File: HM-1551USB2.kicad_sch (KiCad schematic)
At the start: 21 parts, among them Q1 IRLML6402, U1 USBLC6-2SC6, U2 FT232RL, U3 HM-MOD-UART

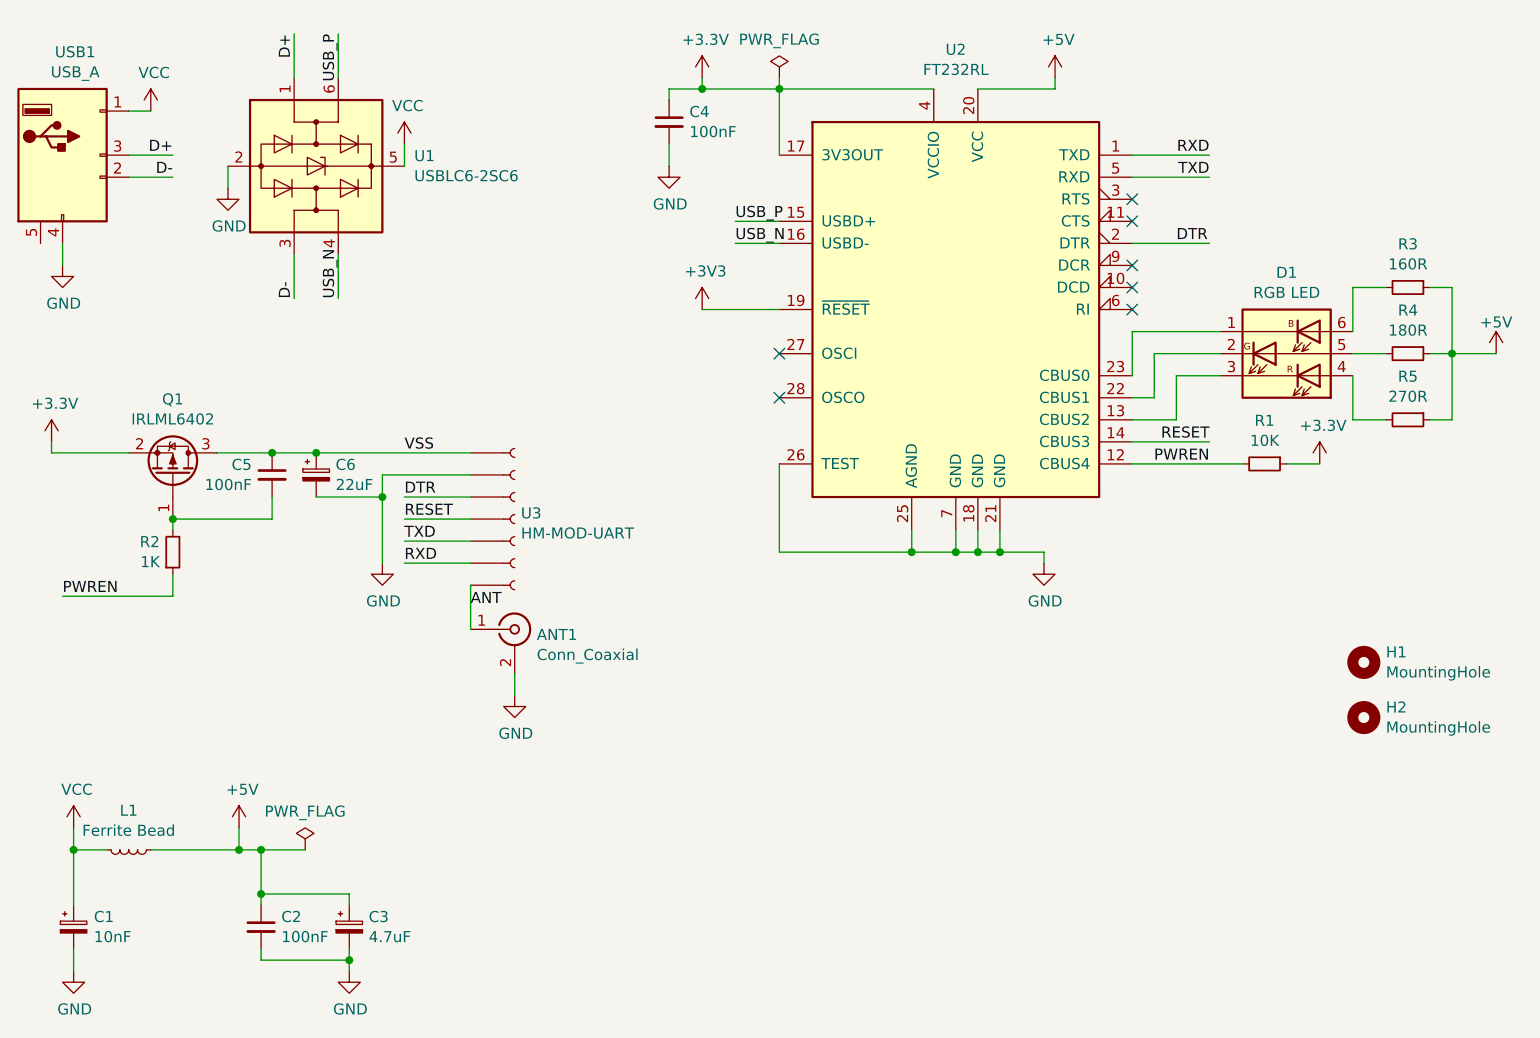
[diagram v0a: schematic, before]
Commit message: Update component properties and fill BOM
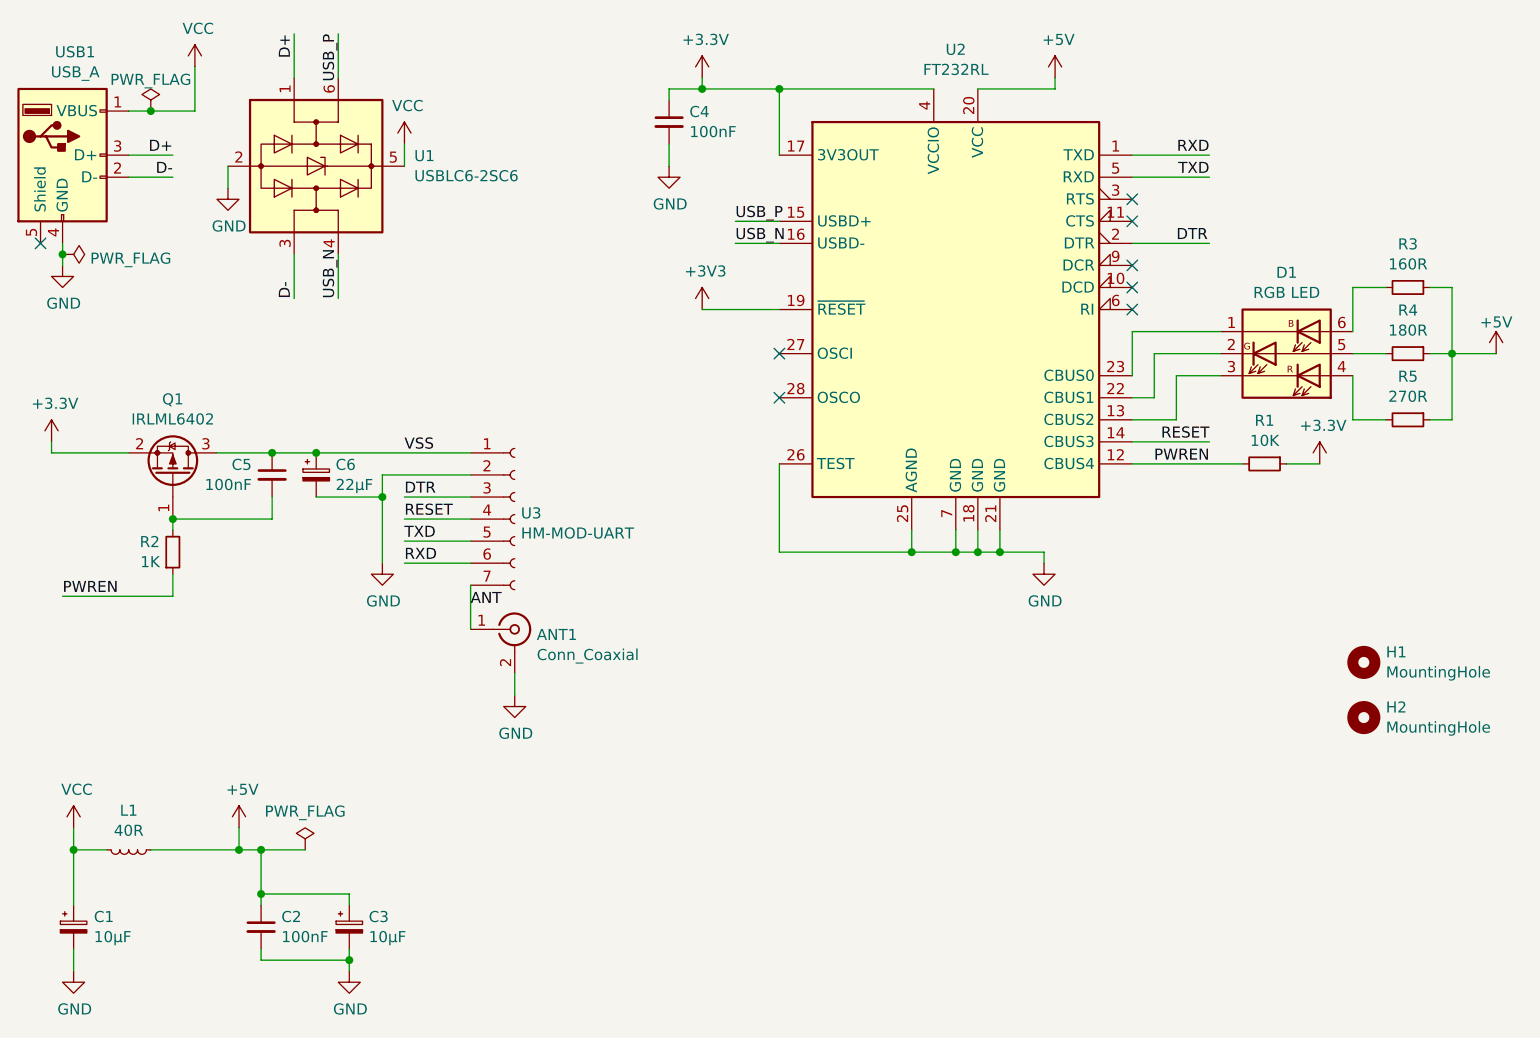
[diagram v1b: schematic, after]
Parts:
- ANT1: LCSC (none) -> C914558; PN (none) -> SMA-KE-P903
- C1: value 10nF -> 10µF; symbol Device:CP_Small -> Device:C_Polarized_Small; LCSC (none) -> C7177; PN (none) -> TAJA106K010RNJ
- C2, C4, C5: LCSC (none) -> C307360; PN (none) -> CL21B104KBFWPNE
- C3: value 4.7uF -> 10µF; symbol Device:CP_Small -> Device:C_Polarized_Small; LCSC (none) -> C7177; PN (none) -> TAJA106K010RNJ
- C6: value 22uF -> 22µF; symbol Device:CP_Small -> Device:C_Polarized_Small; LCSC (none) -> C130377; PN (none) -> 293D226X9016C2TE3
- D1: LCSC (none) -> C1322332; PN (none) -> TJ-S5050UG2W6TLCBRG-A5
- H1, H2: now left out of the parts list
- L1: value Ferrite Bead -> 40R; LCSC (none) -> C2661672; PN (none) -> MMZ2012S400AT000
- Q1: LCSC (none) -> C2593; PN (none) -> IRLML6402TRPBF
- R1: LCSC (none) -> C869153; PN (none) -> RT0805FRE0710KL
- R2: LCSC (none) -> C144087; PN (none) -> AF0603FR-071KL
- R3: LCSC (none) -> C228326; PN (none) -> AC0805FR-07160RL
- R4: LCSC (none) -> C228347; PN (none) -> AC0805FR-07180RL
- R5: LCSC (none) -> C228675; PN (none) -> AC0805FR-07270RL
- U1: LCSC (none) -> C7519; PN (none) -> USBLC6-2SC6
- U2: symbol HM-1551USB2-rescue:FT232RL-Interface_USB -> Interface_USB:FT232RL; LCSC (none) -> C8690; PN (none) -> FT232RL-REEL
- U3: PN (none) -> HM-MOD-RPI-PCB
- USB1: LCSC (none) -> C46394; PN (none) -> 917-181A102ES60200
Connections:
- no-connect marks 7 -> 8
